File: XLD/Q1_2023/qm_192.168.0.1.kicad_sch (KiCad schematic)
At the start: 113 parts

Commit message: done
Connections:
- net at Splitter717.: now also Splitter718.; no longer Splitter716.
- net at Splitter718.: no longer Splitter717.
- net at Splitter706.: now also Splitter705.; no longer Splitter708.
- net at Splitter710.: now also Splitter709.; no longer Splitter708.
- net at Splitter722.: no longer Splitter721.
- net at Splitter720.: no longer Splitter721.
- net at Splitter707.: no longer Splitter706.
- net at Splitter705.: no longer Splitter706.
- net at Splitter714.: now also Splitter713.
- net at Splitter713.: now also Splitter712.; no longer Splitter714.
- net at Splitter711.: now also Splitter710.
- net at Splitter712.: no longer Splitter713.
- net at Splitter701.: no longer Splitter702.
- net at Splitter703.: no longer Splitter702.
- net at Splitter704.: now also Splitter703.
- new net: Splitter716., Splitter717.
- new net: Splitter715., Splitter717.
- new net: Splitter706., Splitter708.
- new net: Splitter708., Splitter710.
- new net: Splitter721., Splitter722.
- new net: Splitter720., Splitter721.
- new net: Splitter706., Splitter707.
- new net: Splitter713., Splitter715.
- new net: Splitter701., Splitter702.
- new net: Splitter702., Splitter703.
- now unconnected: Splitter703.

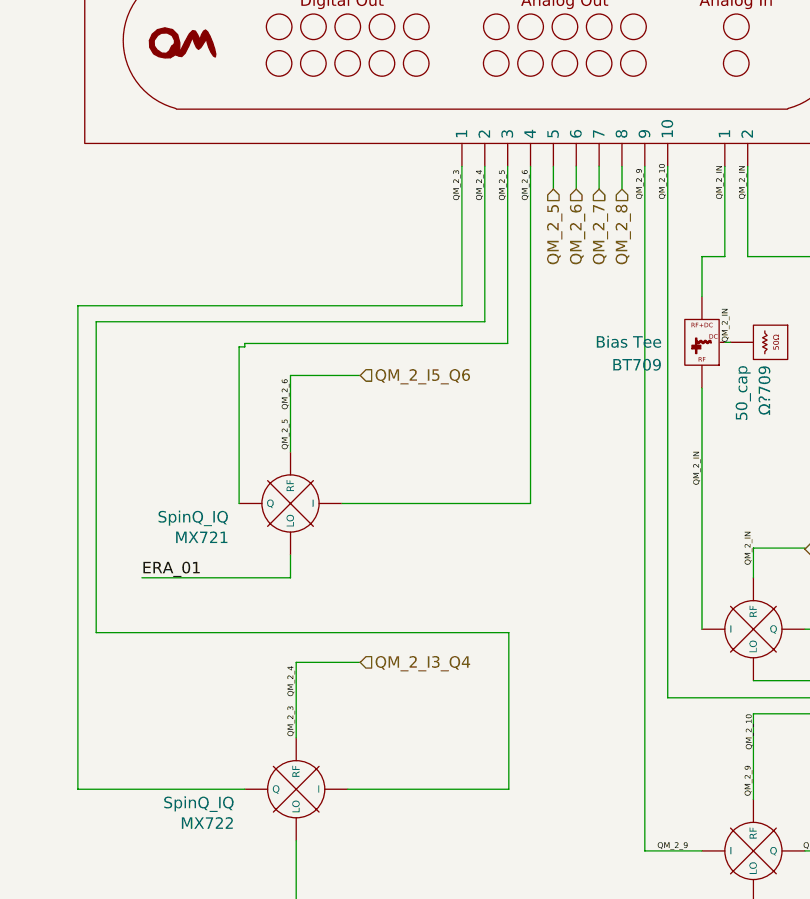
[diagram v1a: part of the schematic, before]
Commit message: Corrected but path not verified
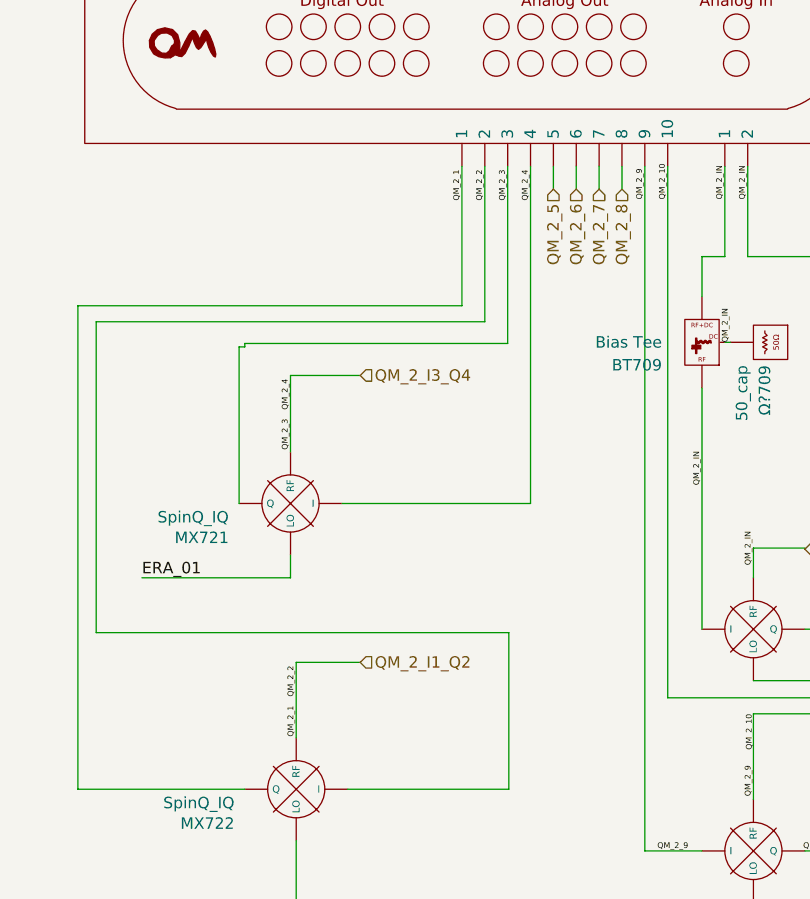
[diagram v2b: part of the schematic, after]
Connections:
- net QM_2_5: no longer MX721. (RF)
- net QM_2_I3_Q4: now also MX721. (RF); no longer MX722. (RF)
- net at Splitter717.: now also Splitter718.; no longer Splitter716.
- net at Splitter718.: no longer Splitter717.
- net at Splitter706.: now also Splitter705.; no longer Splitter708.
- net at Splitter710.: now also Splitter709.; no longer Splitter708.
- net at Splitter722.: no longer Splitter721.
- net at Splitter720.: no longer Splitter721.
- net at Splitter707.: no longer Splitter706.
- net at Splitter705.: no longer Splitter706.
- net at Splitter714.: now also Splitter713.
- net at Splitter713.: now also Splitter712.; no longer Splitter714.
- net at Splitter711.: now also Splitter710.
- net at Splitter712.: no longer Splitter713.
- net at Splitter701.: no longer Splitter702.
- net at Splitter703.: no longer Splitter702.
- net at Splitter704.: now also Splitter703.
- new net: Splitter716., Splitter717.
- new net: Splitter715., Splitter717.
- new net: Splitter706., Splitter708.
- new net: Splitter708., Splitter710.
- new net: Splitter721., Splitter722.
- new net: Splitter720., Splitter721.
- new net: Splitter706., Splitter707.
- new net: Splitter713., Splitter715.
- new net: Splitter701., Splitter702.
- new net: Splitter702., Splitter703.
- new net QM_2_6: OPX706. (LAN)
- new net QM_2_I1_Q2: MX722. (RF), OPX706. (LAN)
- now unconnected: Splitter703.
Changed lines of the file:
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@@
     (effects (font (size 0.64 0.64)) (justify right bottom))
   )
-  (label "QM_2_4" (at 254.635 253.873 90) (fields_autoplaced)
+  (label "QM_2_2" (at 254.635 253.873 90) (fields_autoplaced)
     (effects (font (size 0.64 0.64)) (justify left bottom))
   )
@@
     (effects (font (size 0.64 0.64)) (justify left bottom))
   )
-  (label "QM_2_6" (at 254 221.996 90) (fields_autoplaced)
+  (label "QM_2_4" (at 254 221.996 90) (fields_autoplaced)
     (effects (font (size 0.64 0.64)) (justify left bottom))
   )
@@
     (effects (font (size 0.64 0.64)) (justify left bottom))
   )
-  (label "QM_2_5" (at 254 226.441 90) (fields_autoplaced)
+  (label "QM_2_3" (at 254 226.441 90) (fields_autoplaced)
     (effects (font (size 0.64 0.64)) (justify left bottom))
   )
@@
     (effects (font (size 0.64 0.64)) (justify right bottom))
   )
-  (label "QM_2_5" (at 278.13 198.755 90) (fields_autoplaced)
+  (label "QM_2_3" (at 278.13 198.755 90) (fields_autoplaced)
     (effects (font (size 0.64 0.64)) (justify left bottom))
   )
@@
     (effects (font (size 0.64 0.64)) (justify left bottom))
   )
-  (label "QM_2_6" (at 280.67 198.755 90) (fields_autoplaced)
+  (label "QM_2_4" (at 280.67 198.755 90) (fields_autoplaced)
     (effects (font (size 0.64 0.64)) (justify left bottom))
   )
@@
     (effects (font (size 0.64 0.64)) (justify left bottom))
   )
-  (label "QM_2_3" (at 273.05 198.755 90) (fields_autoplaced)
+  (label "QM_2_1" (at 273.05 198.755 90) (fields_autoplaced)
     (effects (font (size 0.64 0.64)) (justify left bottom))
   )
@@
     (effects (font (size 0.64 0.64)) (justify left bottom))
   )
-  (label "QM_2_3" (at 254.635 258.318 90) (fields_autoplaced)
+  (label "QM_2_1" (at 254.635 258.318 90) (fields_autoplaced)
     (effects (font (size 0.64 0.64)) (justify left bottom))
   )
@@
     (effects (font (size 0.64 0.64)) (justify left bottom))
   )
-  (label "QM_2_4" (at 275.59 198.755 90) (fields_autoplaced)
+  (label "QM_2_2" (at 275.59 198.755 90) (fields_autoplaced)
     (effects (font (size 0.64 0.64)) (justify left bottom))
   )
@@
     (effects (font (size 1.27 1.27)) (justify left))
   )
-  (hierarchical_label "QM_2_I3_Q4" (shape input) (at 261.747 250.063 0) (fields_autoplaced)
+  (hierarchical_label "QM_2_I1_Q2" (shape input) (at 261.747 250.063 0) (fields_autoplaced)
     (effects (font (size 1.27 1.27)) (justify left))
   )
@@
     (effects (font (size 1.27 1.27)) (justify left))
   )
-  (hierarchical_label "QM_2_I5_Q6" (shape input) (at 261.747 218.186 0) (fields_autoplaced)
-    (effects (font (size 1.27 1.27)) (justify left))
-  )
+  (hierarchical_label "QM_2_I3_Q4" (shape input) (at 261.747 218.186 0) (fields_autoplaced)
+    (effects (font (size 1.27 1.27)) (justify left))
+  )

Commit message: filter fixed'
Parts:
- renumbered BT716 to BT?, BT710 to BT?, BT709 to BT?, BT702 to BT?, BT708 to BT?, BT712 to BT?, BT707 to BT?, BT715 to BT?, BT701 to BT?, BT703 to BT?, BT711 to BT?, BT704 to BT?, BT706 to BT?, BT714 to BT?, BT705 to BT?, BT713 to BT?, LO706 to LO?, LO710 to LO?, LO713 to LO?, LO715 to LO?, LO702 to LO?, LO714 to LO?, LO707 to LO?, LO705 to LO?, LO708 to LO?, LO701 to LO?, LO712 to LO?, LO709 to LO?, LO704 to LO?, LO703 to LO?, LO711 to LO?, OPX701 to OPX?, OPX709 to OPX?, OPX704 to OPX?, OPX708 to OPX?, OPX706 to OPX?, OPX703 to OPX?, OPX707 to OPX?, OPX702 to OPX?, OPX705 to OPX?, Splitter717 to Splitter?, Splitter716 to Splitter?, Splitter708 to Splitter?, Splitter721 to Splitter?, Splitter706 to Splitter?, Splitter714 to Splitter?, Splitter719 to Splitter?, Splitter707 to Splitter?, Splitter711 to Splitter?, Splitter715 to Splitter?, Splitter713 to Splitter?, Splitter718 to Splitter?, Splitter709 to Splitter?, Splitter702 to Splitter?, Splitter712 to Splitter?, Splitter704 to Splitter?, Splitter701 to Splitter?, Splitter722 to Splitter?, Splitter705 to Splitter?, Splitter710 to Splitter?, Splitter703 to Splitter?, Splitter720 to Splitter?, Ω?712 to Ω?, Ω?713 to Ω?, Ω?710 to Ω?, Ω?702 to Ω?, Ω?704 to Ω?, Ω?716 to Ω?, Ω?715 to Ω?, Ω?708 to Ω?, Ω?703 to Ω?, Ω?706 to Ω?, Ω?714 to Ω?, Ω?705 to Ω?, Ω?711 to Ω?, Ω?709 to Ω?, Ω?701 to Ω?, Ω?707 to Ω?
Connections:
- net ERA_01: no longer LO?.
- net ERA_02: no longer LO?.
- net ERA_03: no longer LO?.
- net ERA_04: no longer LO?.
- net LO_01: no longer LO?.
- net LO_02: no longer LO?.
- net LO_03: no longer LO?.
- net LO_04: no longer LO?.
- net LO_05: no longer LO?.
- net LO_06: no longer LO?.
- net at Splitter?.: now also Splitter?.; no longer Splitter?. (x4)
- net at Splitter?.: no longer Splitter?. (x8)
- net at Splitter?.: now also Splitter?. (x3)
- new net: Splitter?., Splitter?. (x10)
- now unconnected: Splitter?.
